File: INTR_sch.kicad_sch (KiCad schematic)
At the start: 6 parts, among them U18 8259A

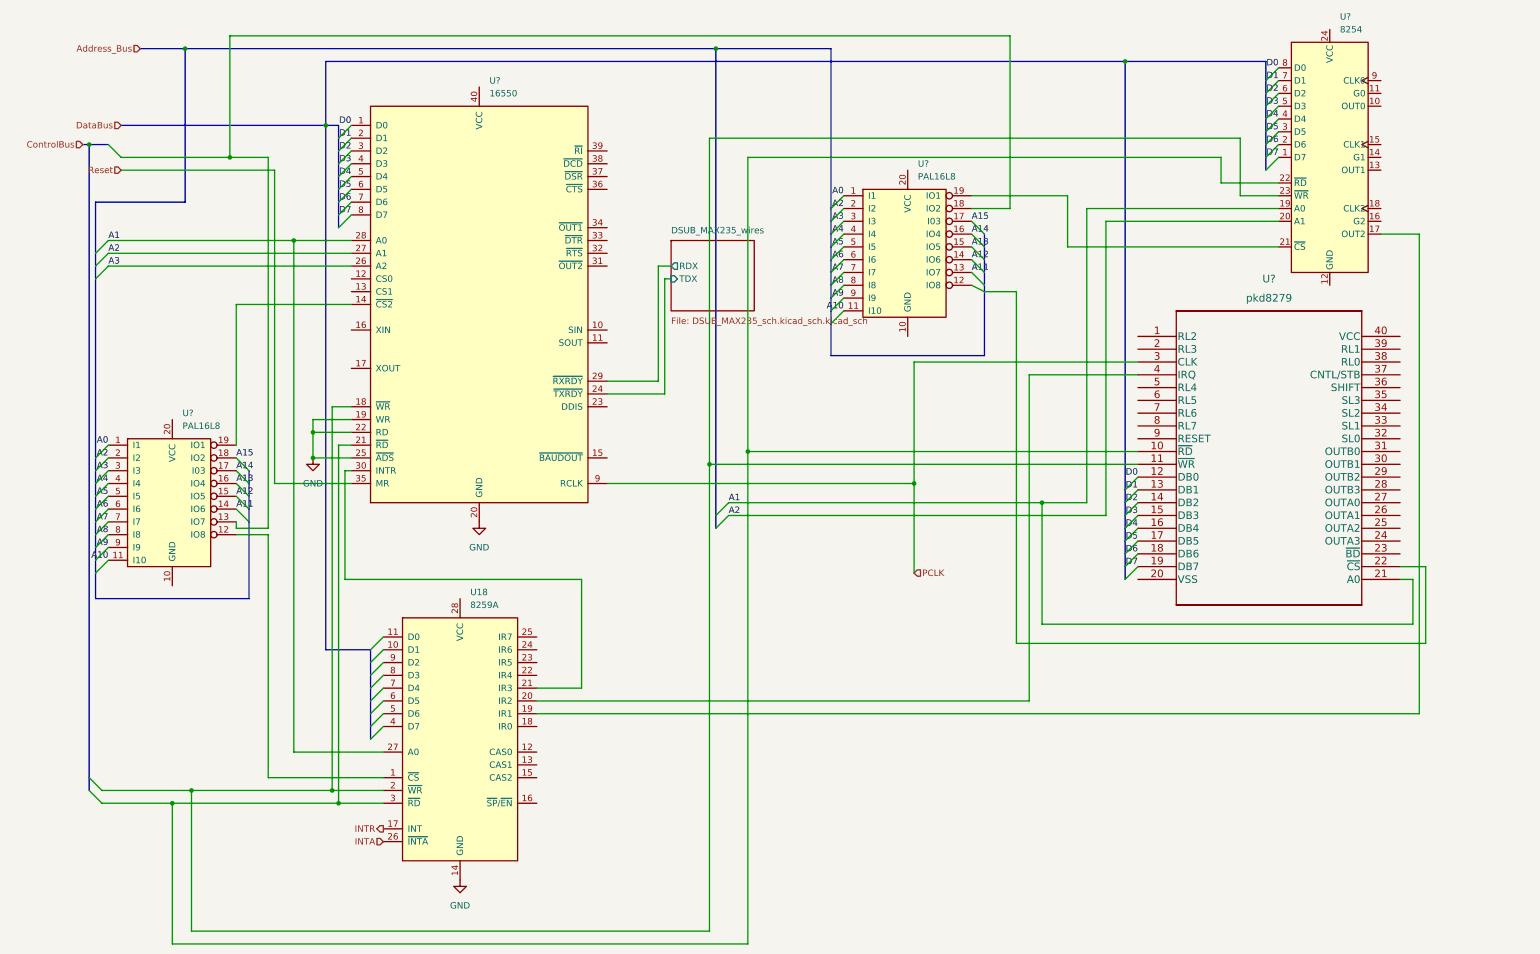
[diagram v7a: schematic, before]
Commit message: Added headers to the necessary pins, and created IO device sheet
Added headers for the three chips and for the busses. Also created and started to address  decode the actual IO components.
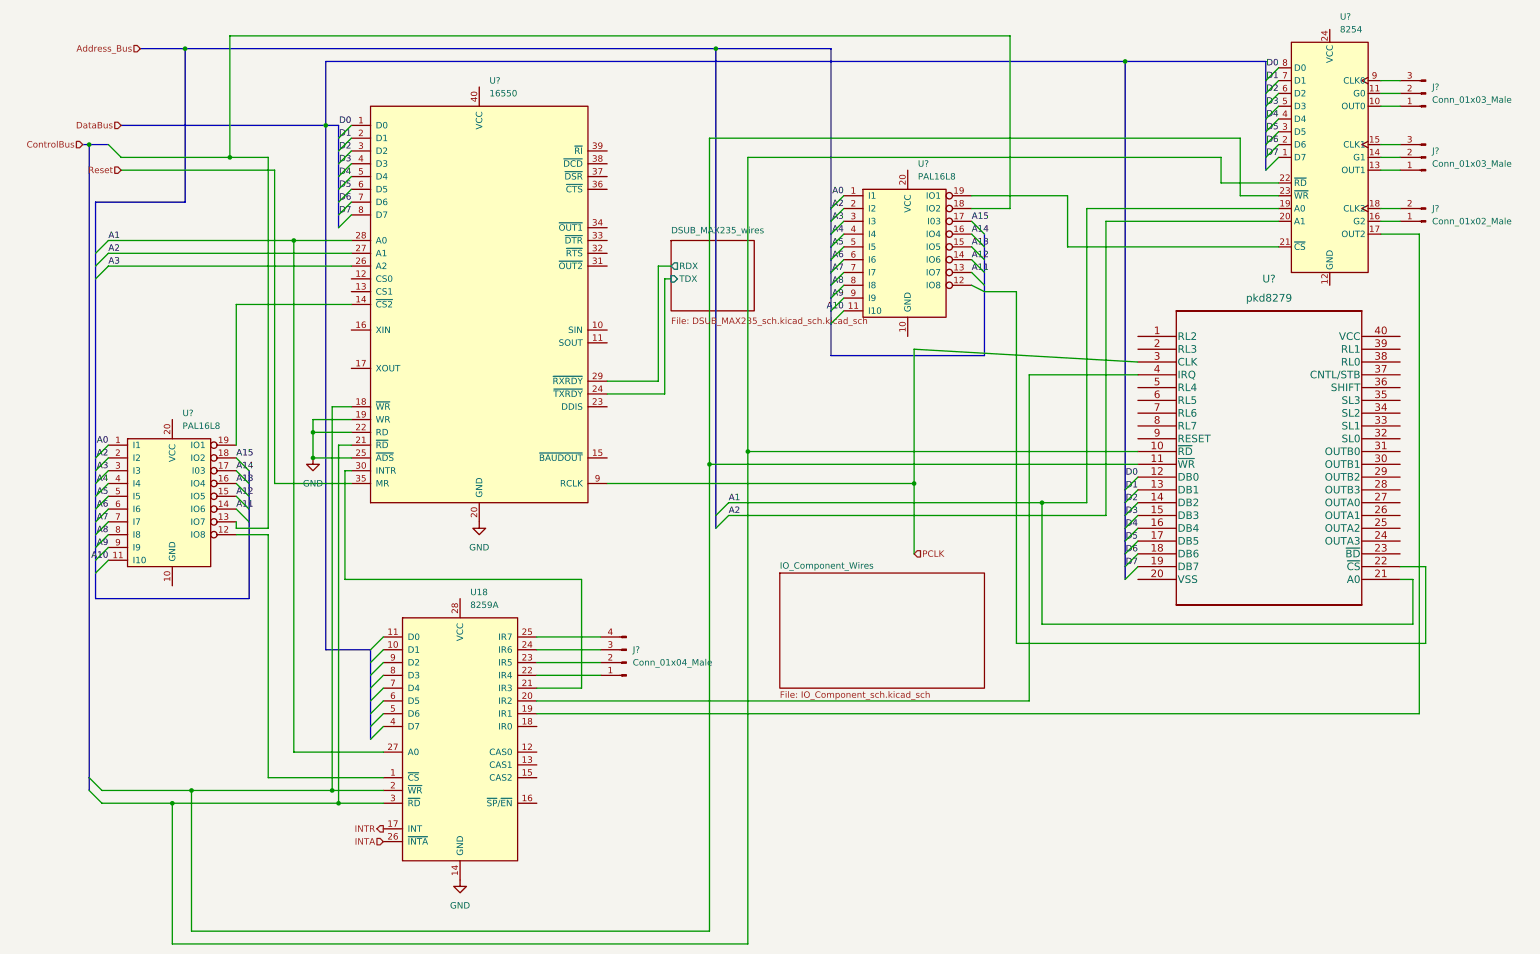
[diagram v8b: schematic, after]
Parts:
- added J?: Conn_01x02_Male, symbol Connector:Conn_01x02_Male
- added J?: Conn_01x04_Male, symbol Connector:Conn_01x04_Male
- added J? (x2): Conn_01x03_Male, symbol Connector:Conn_01x03_Male
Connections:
- net at U18.22 (IR4): now also J?.1 (Pin_1)
- net at U18.23 (IR5): now also J?.2 (Pin_2)
- net at U18.24 (IR6): now also J?.3 (Pin_3)
- net at U18.25 (IR7): now also J?.4 (Pin_4)
- net at U?.10 (OUT0): now also J?.1 (Pin_1)
- net at U?.11 (G0): now also J?.2 (Pin_2)
- net at U?.13 (OUT1): now also J?.1 (Pin_1)
- net at U?.14 (G1): now also J?.2 (Pin_2)
- net at U?.15 (CLK1): now also J?.3 (Pin_3)
- net at U?.16 (G2): now also J?.1 (Pin_1)
- net at U?.18 (CLK2): now also J?.2 (Pin_2)
- net at U?.9 (CLK0): now also J?.3 (Pin_3)
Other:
- added sheet IO_Component_Wires (IO_Component_sch.kicad_sch)
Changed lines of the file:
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@@
+    (stroke (width 0) (type default) (color 0 0 0 0))
+  )
+  (wire (pts (xy 274.32 41.91) (xy 278.13 41.91))
     (stroke (width 0) (type default) (color 0 0 0 0))
   )
@@
     (stroke (width 0) (type default) (color 0 0 0 0))
   )
+  (wire (pts (xy 274.32 49.53) (xy 278.13 49.53))
+    (stroke (width 0) (type default) (color 0 0 0 0))
+  )
   (bus (pts (xy 73.66 142.24) (xy 73.66 139.7))
     (stroke (width 0) (type default) (color 0 0 0 0))
@@
     (stroke (width 0) (type default) (color 0 0 0 0))
   )
-  (wire (pts (xy 226.06 80.01) (xy 181.61 80.01))
+  (wire (pts (xy 226.06 80.01) (xy 181.61 77.47))
     (stroke (width 0) (type default) (color 0 0 0 0))
   )
@@
     (stroke (width 0) (type default) (color 0 0 0 0))
   )
+  (wire (pts (xy 274.32 26.67) (xy 278.13 26.67))
+    (stroke (width 0) (type default) (color 0 0 0 0))
+  )
+  (wire (pts (xy 274.32 52.07) (xy 278.13 52.07))
+    (stroke (width 0) (type default) (color 0 0 0 0))
+  )
   (bus (pts (xy 67.31 45.72) (xy 67.31 48.26))
     (stroke (width 0) (type default) (color 0 0 0 0))
@@
     (stroke (width 0) (type default) (color 0 0 0 0))
   )
+  (wire (pts (xy 274.32 36.83) (xy 278.13 36.83))
+    (stroke (width 0) (type default) (color 0 0 0 0))
+  )
   (wire (pts (xy 58.42 55.88) (xy 58.42 157.48))
     (stroke (width 0) (type default) (color 0 0 0 0))
@@
     (stroke (width 0) (type default) (color 0 0 0 0))
   )
-  (wire (pts (xy 181.61 80.01) (xy 181.61 104.14))
+  (wire (pts (xy 181.61 77.47) (xy 181.61 104.14))
     (stroke (width 0) (type default) (color 0 0 0 0))
   )
@@
     (stroke (width 0) (type default) (color 0 0 0 0))
   )
+  (wire (pts (xy 181.61 104.14) (xy 181.61 118.11))
+    (stroke (width 0) (type default) (color 0 0 0 0))
+  )
   (bus (pts (xy 73.66 149.86) (xy 73.66 147.32))
     (stroke (width 0) (type default) (color 0 0 0 0))
@@
     (stroke (width 0) (type default) (color 0 0 0 0))
   )
+  (wire (pts (xy 106.68 137.16) (xy 119.38 137.16))
+    (stroke (width 0) (type default) (color 0 0 0 0))
+  )
   (bus (pts (xy 64.77 33.02) (xy 67.31 33.02))
     (stroke (width 0) (type default) (color 0 0 0 0))
@@
     (stroke (width 0) (type default) (color 0 0 0 0))
   )
+  (wire (pts (xy 106.68 142.24) (xy 119.38 142.24))
+    (stroke (width 0) (type default) (color 0 0 0 0))
+  )
   (wire (pts (xy 226.06 82.55) (xy 204.47 82.55))
     (stroke (width 0) (type default) (color 0 0 0 0))
@@
     (stroke (width 0) (type default) (color 0 0 0 0))
   )
+  (wire (pts (xy 274.32 29.21) (xy 278.13 29.21))
+    (stroke (width 0) (type default) (color 0 0 0 0))
+  )
   (wire (pts (xy 204.47 82.55) (xy 204.47 147.32))
     (stroke (width 0) (type default) (color 0 0 0 0))
@@
     (stroke (width 0) (type default) (color 0 0 0 0))
   )
+  (wire (pts (xy 274.32 24.13) (xy 278.13 24.13))
+    (stroke (width 0) (type default) (color 0 0 0 0))
+  )
   (wire (pts (xy 140.97 100.33) (xy 226.06 100.33))
     (stroke (width 0) (type default) (color 0 0 0 0))
@@
     (stroke (width 0) (type default) (color 0 0 0 0))
   )
+  (wire (pts (xy 106.68 134.62) (xy 119.38 134.62))
+    (stroke (width 0) (type default) (color 0 0 0 0))
+  )
   (wire (pts (xy 148.59 97.79) (xy 148.59 39.37))
     (stroke (width 0) (type default) (color 0 0 0 0))
@@
     (stroke (width 0) (type default) (color 0 0 0 0))
   )
+  (wire (pts (xy 106.68 139.7) (xy 119.38 139.7))
+    (stroke (width 0) (type default) (color 0 0 0 0))
+  )
   (bus (pts (xy 165.1 52.07) (xy 165.1 54.61))
     (stroke (width 0) (type default) (color 0 0 0 0))
@@
     (stroke (width 0) (type default) (color 0 0 0 0))
   )
-  (wire (pts (xy 181.61 104.14) (xy 181.61 121.92))
-    (stroke (width 0) (type default) (color 0 0 0 0))
-  )
   (bus (pts (xy 142.24 110.49) (xy 142.24 113.03))
+    (stroke (width 0) (type default) (color 0 0 0 0))
+  )
+  (wire (pts (xy 274.32 39.37) (xy 278.13 39.37))
     (stroke (width 0) (type default) (color 0 0 0 0))
   )
@@
     (effects (font (size 1.27 1.27)) (justify right))
   )
-  (hierarchical_label "PCLK" (shape input) (at 181.61 121.92 0)
+  (hierarchical_label "PCLK" (shape input) (at 181.61 118.11 0)
     (effects (font (size 1.27 1.27)) (justify left))
   )
@@
     (pin "1")
   )
+  (symbol (lib_id "Connector:Conn_01x02_Male") (at 283.21 52.07 180) (unit 1)
+    (in_bom yes) (on_board yes) (fields_autoplaced)
+    (property "Reference" "J?" (id 0) (at 284.48 49.5299 0)
+      (effects (font (size 1.27 1.27)) (justify right))
+    )
+    (property "Value" "Conn_01x02_Male" (id 1) (at 284.48 52.0699 0)
+      (effects (font (size 1.27 1.27)) (justify right))
+    )
+    (property "Footprint" "" (id 2) (at 283.21 52.07 0)
+      (effects (font (size 1.27 1.27)) hide)
+    )
+    (property "Datasheet" "~" (id 3) (at 283.21 52.07 0)
+      (effects (font (size 1.27 1.27)) hide)
+    )
+    (pin "1")
+    (pin "2")
+  )
+  (symbol (lib_id "Connector:Conn_01x04_Male") (at 124.46 139.7 180) (unit 1)
+    (in_bom yes) (on_board yes) (fields_autoplaced)
+    (property "Reference" "J?" (id 0) (at 125.73 137.1599 0)
+      (effects (font (size 1.27 1.27)) (justify right))
+    )
+    (property "Value" "Conn_01x04_Male" (id 1) (at 125.73 139.6999 0)
+      (effects (font (size 1.27 1.27)) (justify right))
+    )
+    (property "Footprint" "" (id 2) (at 124.46 139.7 0)
+      (effects (font (size 1.27 1.27)) hide)
+    )
+    (property "Datasheet" "~" (id 3) (at 124.46 139.7 0)
+      (effects (font (size 1.27 1.27)) hide)
+    )
+    (pin "1")
+    (pin "2")
+    (pin "3")
+    (pin "4")
+  )
   (symbol (lib_id "Logic_Programmable:PAL16L8") (at 34.29 109.22 0) (unit 1)
     (in_bom yes) (on_board yes) (fields_autoplaced)
@@
     (pin "8")
     (pin "9")
+  )
+  (symbol (lib_id "Connector:Conn_01x03_Male") (at 283.21 39.37 180) (unit 1)
+    (in_bom yes) (on_board yes) (fields_autoplaced)
+    (property "Reference" "J?" (id 0) (at 284.48 38.0999 0)
+      (effects (font (size 1.27 1.27)) (justify right))
+    )
+    (property "Value" "Conn_01x03_Male" (id 1) (at 284.48 40.6399 0)
+      (effects (font (size 1.27 1.27)) (justify right))
+    )
+    (property "Footprint" "" (id 2) (at 283.21 39.37 0)
+      (effects (font (size 1.27 1.27)) hide)
+    )
+    (property "Datasheet" "~" (id 3) (at 283.21 39.37 0)
+      (effects (font (size 1.27 1.27)) hide)
+    )
+    (pin "1")
+    (pin "2")
+    (pin "3")
   )
   (symbol (lib_id "pkd8279:pkd8279") (at 226.06 74.93 0) (unit 1)
@@
     (pin "1")
   )
+  (symbol (lib_id "Connector:Conn_01x03_Male") (at 283.21 26.67 180) (unit 1)
+    (in_bom yes) (on_board yes) (fields_autoplaced)
+    (property "Reference" "J?" (id 0) (at 284.48 25.3999 0)
+      (effects (font (size 1.27 1.27)) (justify right))
+    )
+    (property "Value" "Conn_01x03_Male" (id 1) (at 284.48 27.9399 0)
+      (effects (font (size 1.27 1.27)) (justify right))
+    )
+    (property "Footprint" "" (id 2) (at 283.21 26.67 0)
+      (effects (font (size 1.27 1.27)) hide)
+    )
+    (property "Datasheet" "~" (id 3) (at 283.21 26.67 0)
+      (effects (font (size 1.27 1.27)) hide)
+    )
+    (pin "1")
+    (pin "2")
+    (pin "3")
+  )
+  (sheet (at 154.94 121.92) (size 40.64 22.86) (fields_autoplaced)
+    (stroke (width 0.1524) (type solid) (color 0 0 0 0))
+    (fill (color 0 0 0 0.0000))
+    (property "Sheet name" "IO_Component_Wires" (id 0) (at 154.94 121.2084 0)
+      (effects (font (size 1.27 1.27)) (justify left bottom))
+    )
+    (property "Sheet file" "IO_Component_sch.kicad_sch" (id 1) (at 154.94 145.3646 0)
+      (effects (font (size 1.27 1.27)) (justify left top))
+    )
+  )
   (sheet (at 133.35 55.88) (size 16.51 13.97)
